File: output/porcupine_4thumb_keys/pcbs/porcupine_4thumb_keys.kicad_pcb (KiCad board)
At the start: 2 copper layers, 148.2 x 111.9 mm, 56 parts, among them J1 Jumper, J2 Jumper

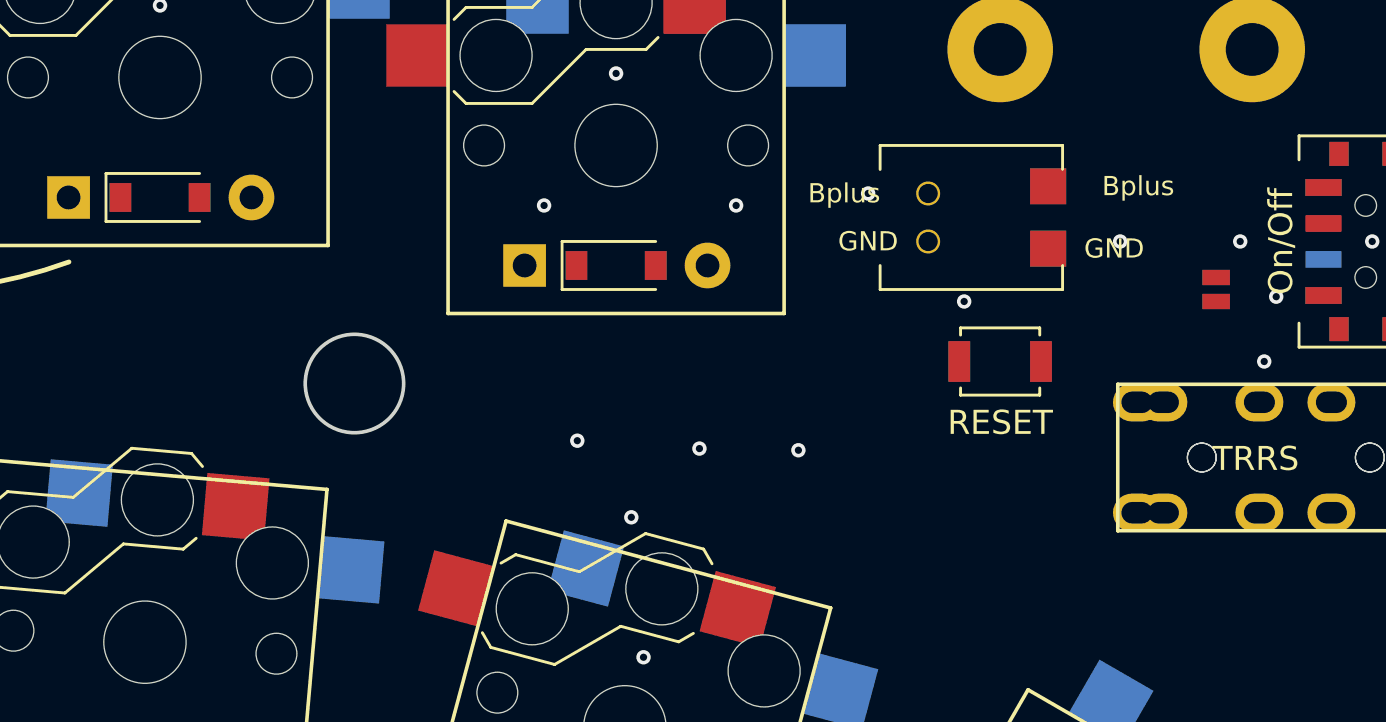
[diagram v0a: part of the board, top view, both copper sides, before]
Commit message: Update input and add manually routed boards
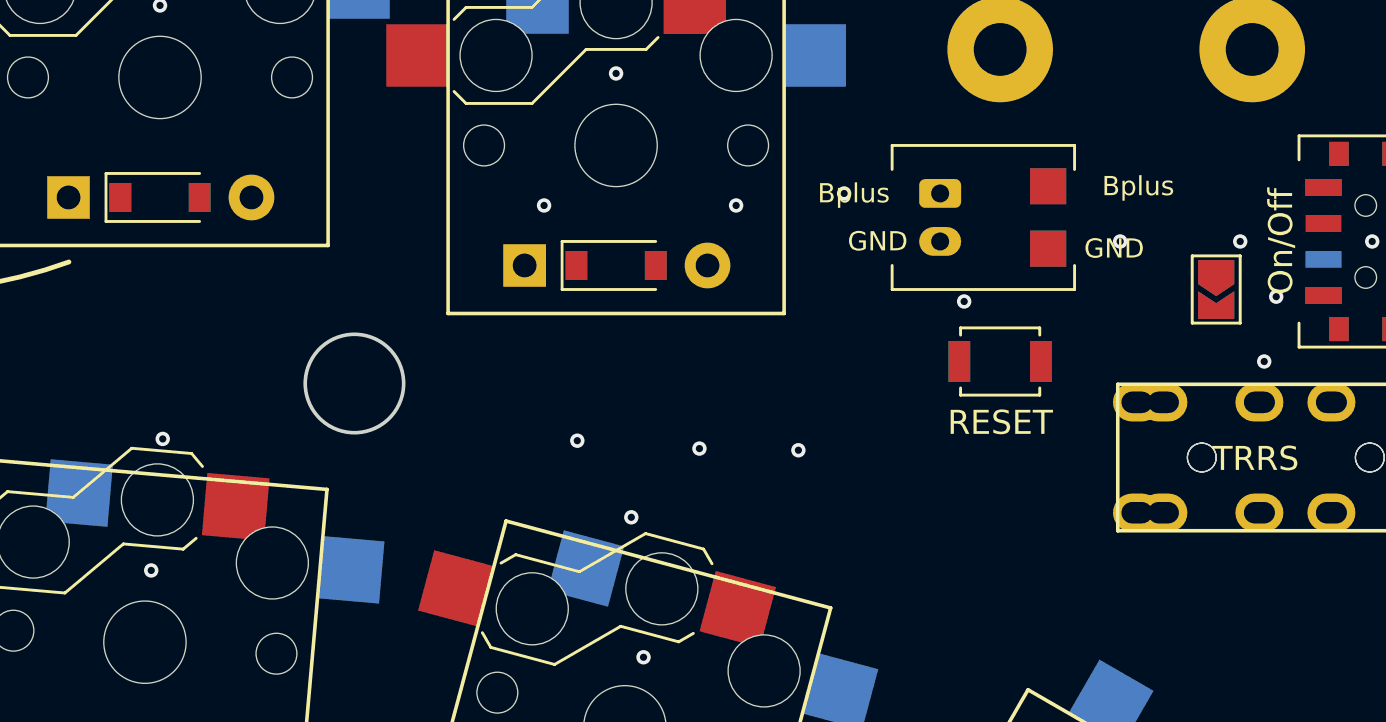
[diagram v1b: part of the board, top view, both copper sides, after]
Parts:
- removed _73, _74: hole, Through Hole
- added _75: hole, Through Hole, F.Cu at (262.4, 122.7)
- added _76: hole, Through Hole, F.Cu at (272.9, 122.7)
- D1, D10, D11, D12, D13, D14, D15, D16, D17, D18, D19, D2, D3, D4, D5, D6, D7, D8, D9: footprint Diode_SMD:D_SOD-123 -> Diode_SMD:SOD-123
- J1: footprint PCM12SMTR -> Jumper:SolderJumper-2_P1.3mm_Open_TrianglePad1.0x1.5mm; moved to B.Cu
- J2: footprint PCM12SMTR -> Jumper:SolderJumper-2_P1.3mm_Open_TrianglePad1.0x1.5mm
- moved _2 0.50 mm to (259.9, 129.7)
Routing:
- net inner_thumb: vias 0 -> 1
- net P19: vias 3 -> 4

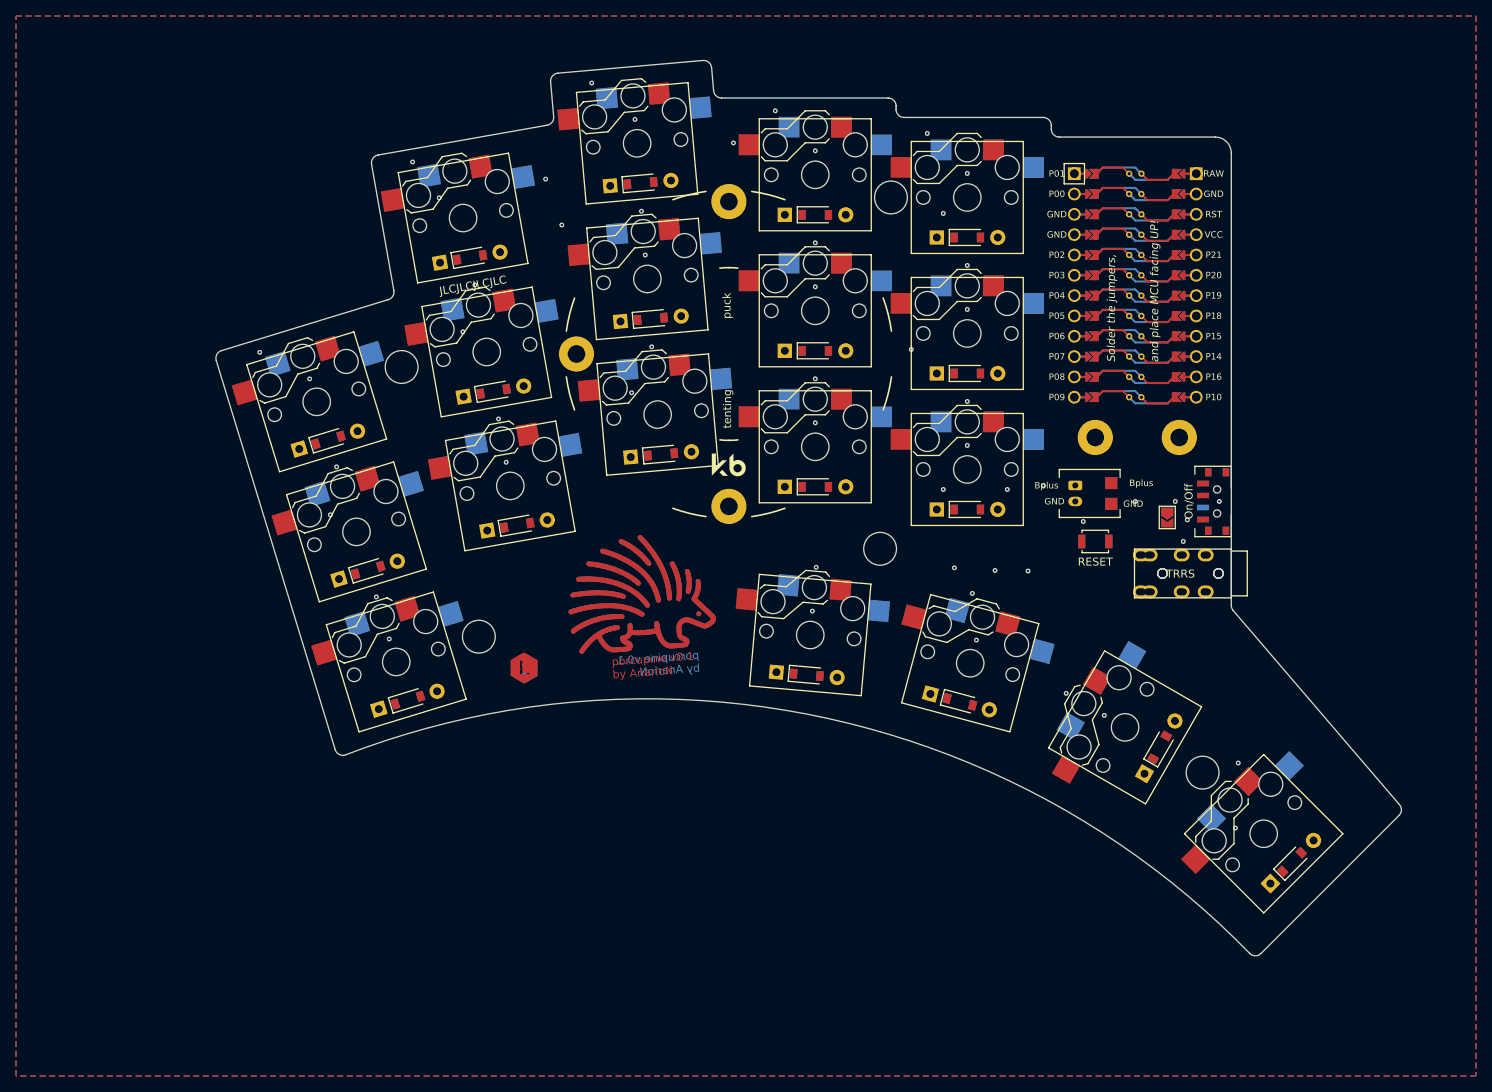
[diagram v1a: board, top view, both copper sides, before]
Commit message: Add new logo
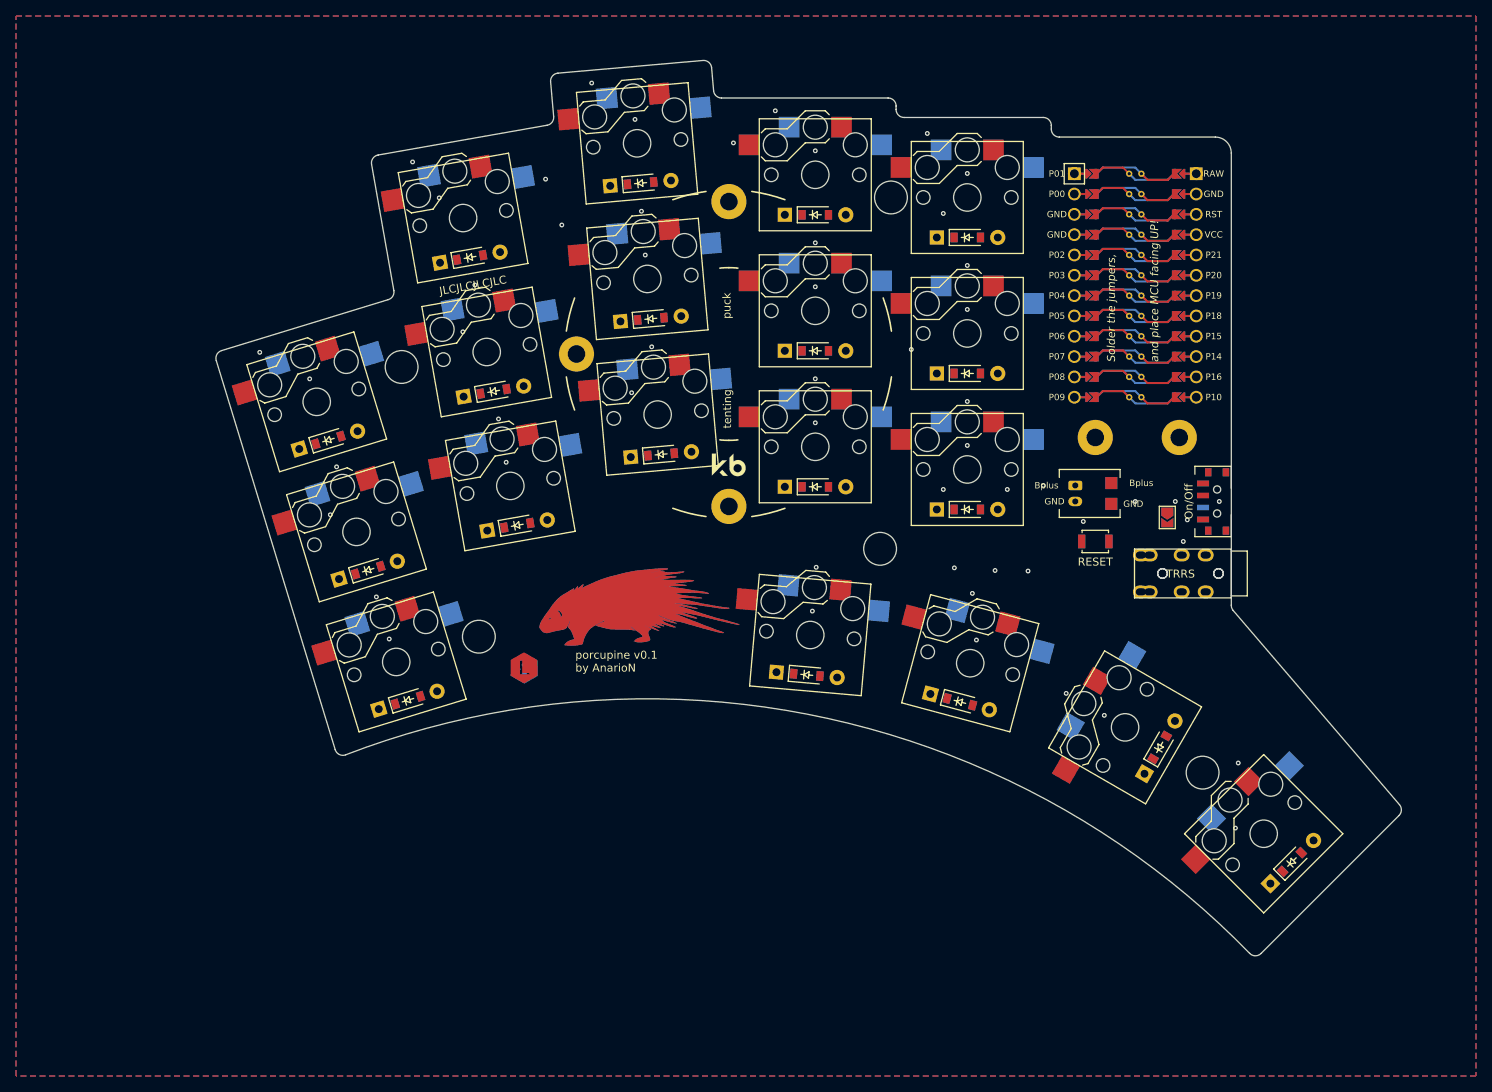
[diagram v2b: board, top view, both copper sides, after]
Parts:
- removed _75, _76: hole, Through Hole
- removed _9: Tenting Puck, Tenting Puck
- added _7: Tenting Puck, Tenting Puck, F.Cu at (216.6, 112.3)
- added _73: hole, Through Hole, F.Cu at (262.4, 122.7)
- added _74: hole, Through Hole, F.Cu at (272.9, 122.7)
- moved LOGO_B 1.75 mm to (205.4, 143.9), turned to 0 degrees
- moved LOGO_F 1.75 mm to (205.4, 143.9), turned to 0 degrees
